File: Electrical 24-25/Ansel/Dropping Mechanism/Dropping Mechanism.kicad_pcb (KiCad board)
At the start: 2 copper layers, 54 x 28 mm, 13 parts, among them J1 Power In, J2 Conn_01x02_Pin, J3 Conn_02x04_Odd_Even, J4 Conn_01x02_Pin, J5 Conn_01x02_Pin, J6 Conn_01x02_Pin

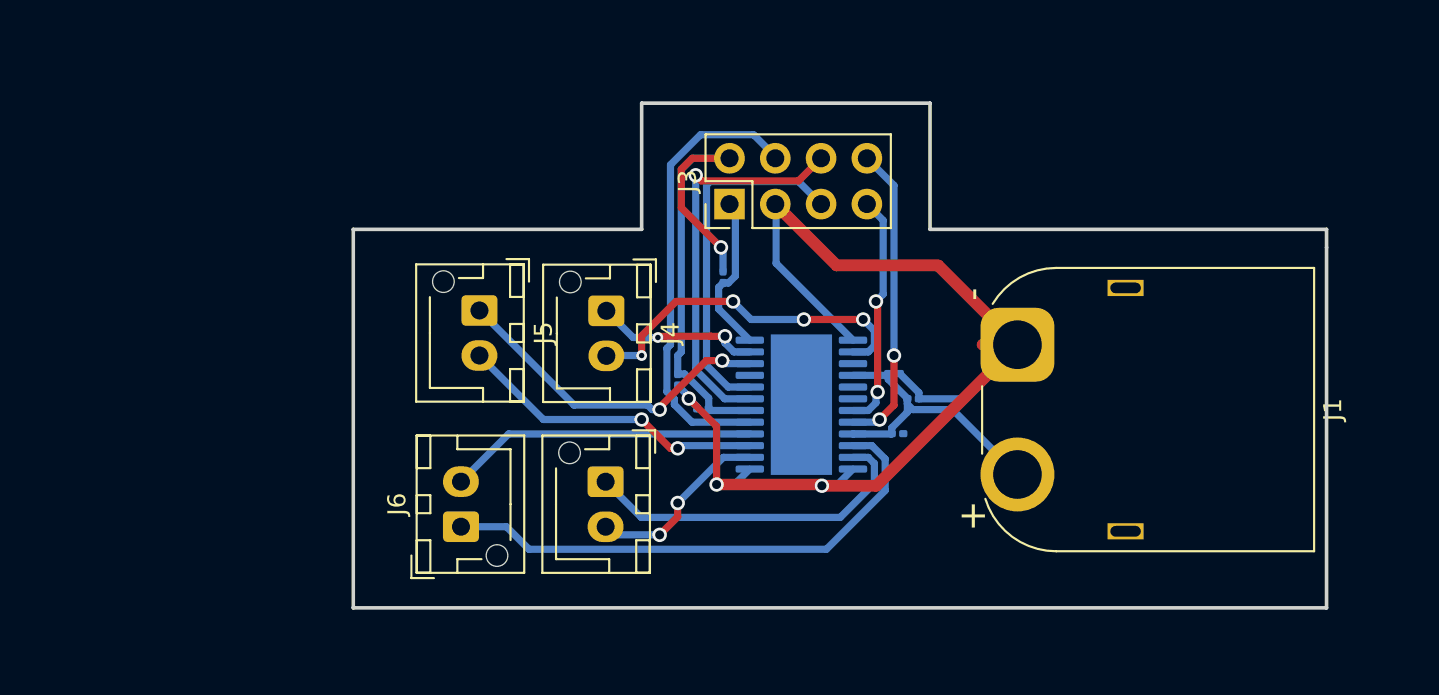
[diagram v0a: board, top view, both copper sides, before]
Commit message: Updates pcb with 0608metric
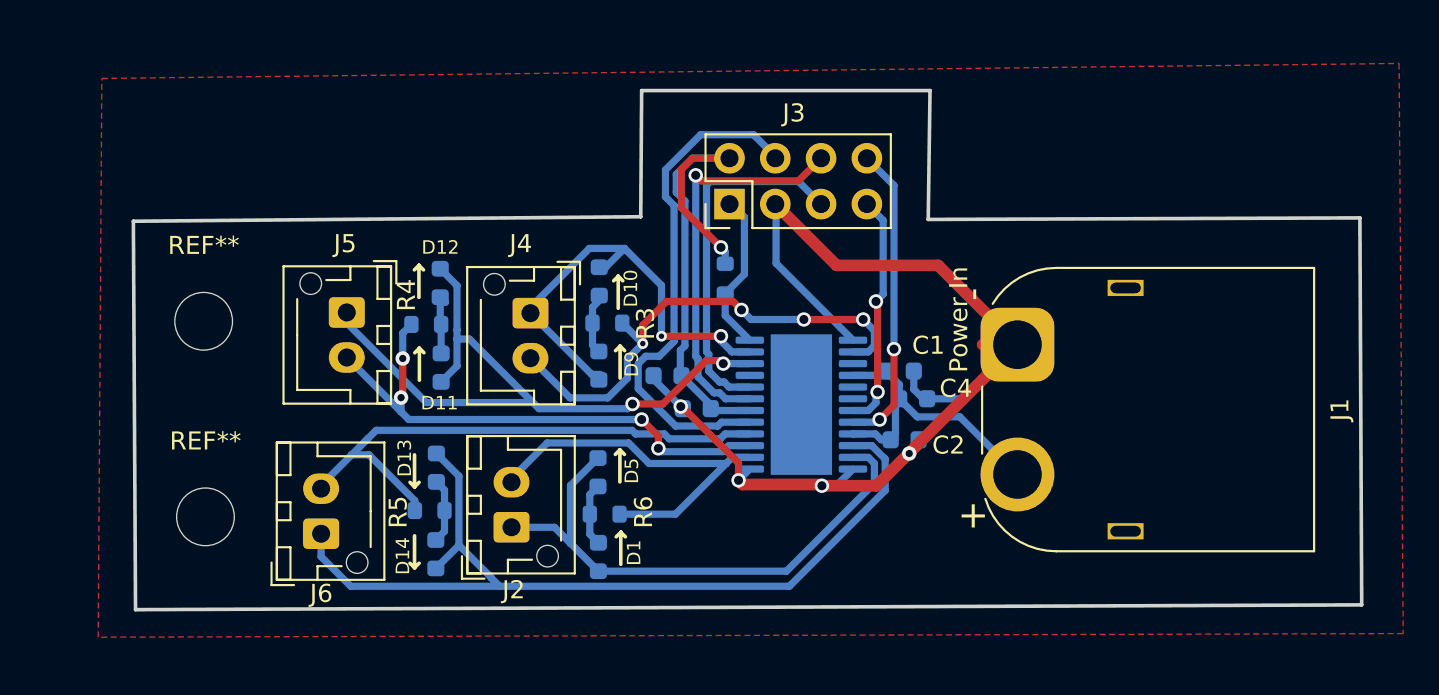
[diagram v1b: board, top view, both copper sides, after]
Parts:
- added D1: D, Diode_SMD:D_0603_1608Metric, B.Cu at (147.6, 65.2)
- added D10: D, Diode_SMD:D_0603_1608Metric, B.Cu at (147.7, 49.9)
- added D11: D, Diode_SMD:D_0603_1608Metric, B.Cu at (138.9, 54.7)
- added D12: D, Diode_SMD:D_0603_1608Metric, B.Cu at (138.8, 50.0)
- added D13: D, Diode_SMD:D_0603_1608Metric, B.Cu at (138.6, 60.2)
- added D14: D, Diode_SMD:D_0603_1608Metric, B.Cu at (138.6, 65.0)
- added D5: D, Diode_SMD:D_0603_1608Metric, B.Cu at (147.6, 60.5)
- added D9: D, Diode_SMD:D_0603_1608Metric, B.Cu at (147.6, 54.6)
- added R3: 0.65k, Resistor_SMD:R_0603_1608Metric, B.Cu at (148.1, 52.2)
- added R4: 0.65k, Resistor_SMD:R_0603_1608Metric, B.Cu at (138.1, 52.3)
- added R5: 0.65k, Resistor_SMD:R_0603_1608Metric, B.Cu at (138.2, 62.6)
- added R6: 0.65k, Resistor_SMD:R_0603_1608Metric, B.Cu at (147.9, 62.8)
- added REF**: MountingHole_3.2mm_M3, MountingHole:MountingHole_3.2mm_M3, F.Cu at (125.7, 52.1)
- added REF**: MountingHole_3.2mm_M3, MountingHole:MountingHole_3.2mm_M3, F.Cu at (125.8, 63.0)
- C1, C2, C4, C5, C6: footprint Capacitor_SMD:C_0201_0603Metric -> Capacitor_SMD:C_0603_1608Metric
- R1: footprint Resistor_SMD:R_0201_0603Metric -> Resistor_SMD:R_0603_1608Metric
- moved J6 7.77 mm to (132.2, 63.9)
- moved J5 7.36 mm to (133.6, 51.6)
- moved J2 5.80 mm to (142.8, 63.5), turned to 90 degrees
- moved J4 4.22 mm to (143.8, 51.6)
- moved C5 0.61 mm to (151.4, 55.1), turned to 0 degrees
- moved C2 0.52 mm to (164.6, 58.7)
- moved C1 0.35 mm to (164.3, 54.9)
- moved C6 0.34 mm to (153.1, 56.9)
- moved R1 0.14 mm to (154.6, 49.7)
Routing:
- net /8: track 29.2 -> 50.9 mm
- net /6: track 18.5 -> 38.8 mm
- net /4: track 9.66 -> 25.1 mm
- net /7: track 17.1 -> 31.2 mm
- net /5: track 17.2 -> 31.2 mm, vias 2 -> 4
- net /2: track 18.9 -> 30.9 mm
- net /1: track 10.4 -> 21.9 mm, vias 2 -> 0
- net /3: track 19.6 -> 27.9 mm
- net Net-(D11-K): track 0.00 -> 3.91 mm
- net Net-(D13-K): track 0.00 -> 3.61 mm
- net Net-(D1-K): track 0.00 -> 3.51 mm
- net Net-(D10-A): track 0.00 -> 3.13 mm
- net /SDI: track 25.2 -> 28.2 mm
- net GND: track 68.1 -> 67.1 mm, vias 3 -> 4
- net /VM1: track 17.1 -> 17.9 mm
- added copper zone on F.Cu, net GND
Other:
- board size 54 x 28 mm -> 68.1 x 28.8 mm

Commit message: Finalized dropping mechanism PCB.
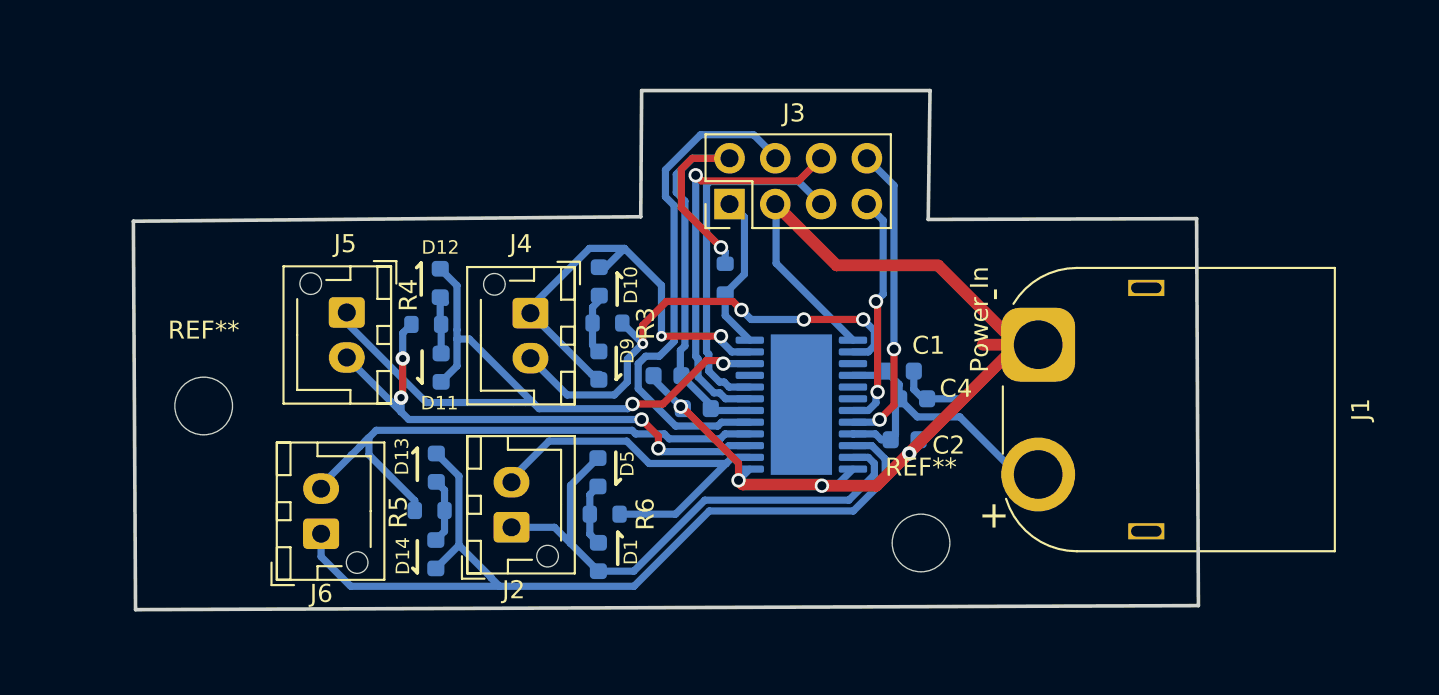
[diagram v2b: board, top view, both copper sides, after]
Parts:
- moved REF** 39.7 mm to (165.5, 64.4)
- moved REF** 4.70 mm to (125.7, 56.8)
- moved J1 1.15 mm to (172.0, 53.4)
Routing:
- net GND: track 67.1 -> 70.6 mm
- net /VM1: track 17.9 -> 19.8 mm
- removed copper zone on F.Cu, net GND
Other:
- board size 68.1 x 28.8 mm -> 59.1 x 28.8 mm

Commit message: Logo added and silkscreen improved
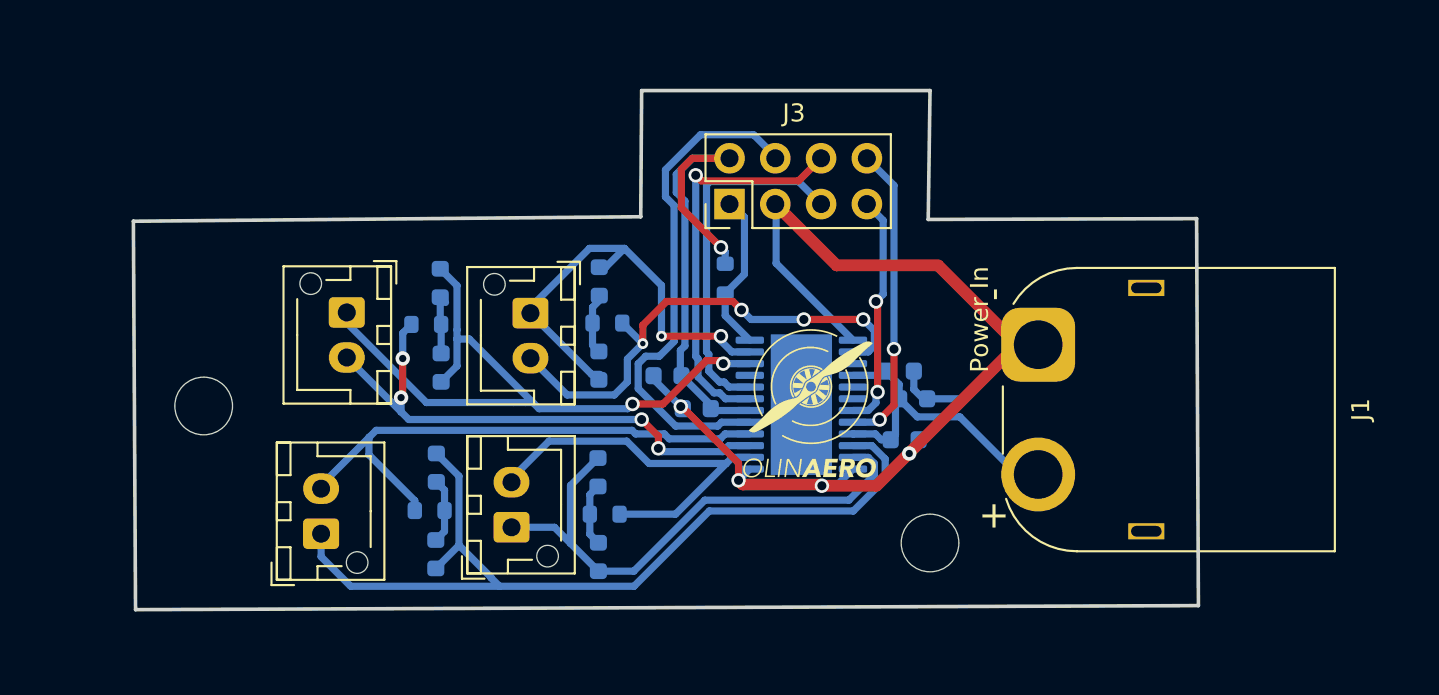
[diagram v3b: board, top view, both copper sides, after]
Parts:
- added G***: LOGO, LOGO, F.Cu at (159.2, 57.5)
- moved REF** 0.50 mm to (166.0, 64.4)
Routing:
- net GND: track 70.6 -> 67.3 mm
- net /5: track 31.2 -> 30.4 mm

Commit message: Final final dropping mechanism pcb.
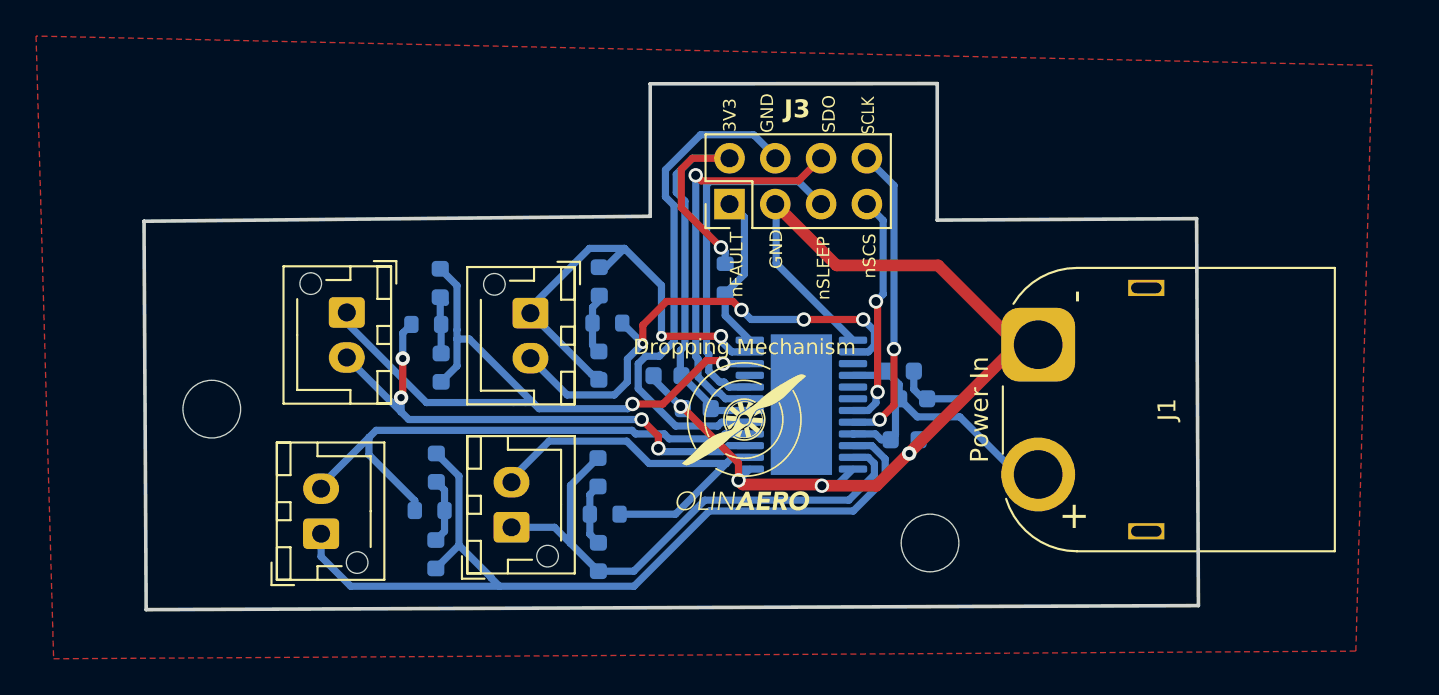
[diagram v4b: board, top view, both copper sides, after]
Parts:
- moved G*** 4.13 mm to (155.6, 59.3)
- moved REF** 0.48 mm to (126.2, 57.0)
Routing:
- added copper zone on F.Cu, net GND
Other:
- board size 59.1 x 28.8 mm -> 58.5 x 29.2 mm
- board text added: "1"
- board text added: "2"
- board text added: "3"
- board text added: "3V3"
- board text added: "4"
- board text added: "5"
- board text added: "6"
- board text added: "7"
- board text added: "8"
- board text added: "Dropping Mechanism"
- board text added: "GND"
- board text added: "M1"
- board text added: "M2"
- board text added: "SCLK"
- board text added: "SDO"
- board text added: "nFAULT"
- board text added: "nSCS"
- board text added: "nSLEEP"
